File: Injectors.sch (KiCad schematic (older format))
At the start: 36 parts, among them Q1 435M9395, Q2 435M9395, Q3 435M9395, Q4 435M9395, Q5 435M9395, Q6 435M9395

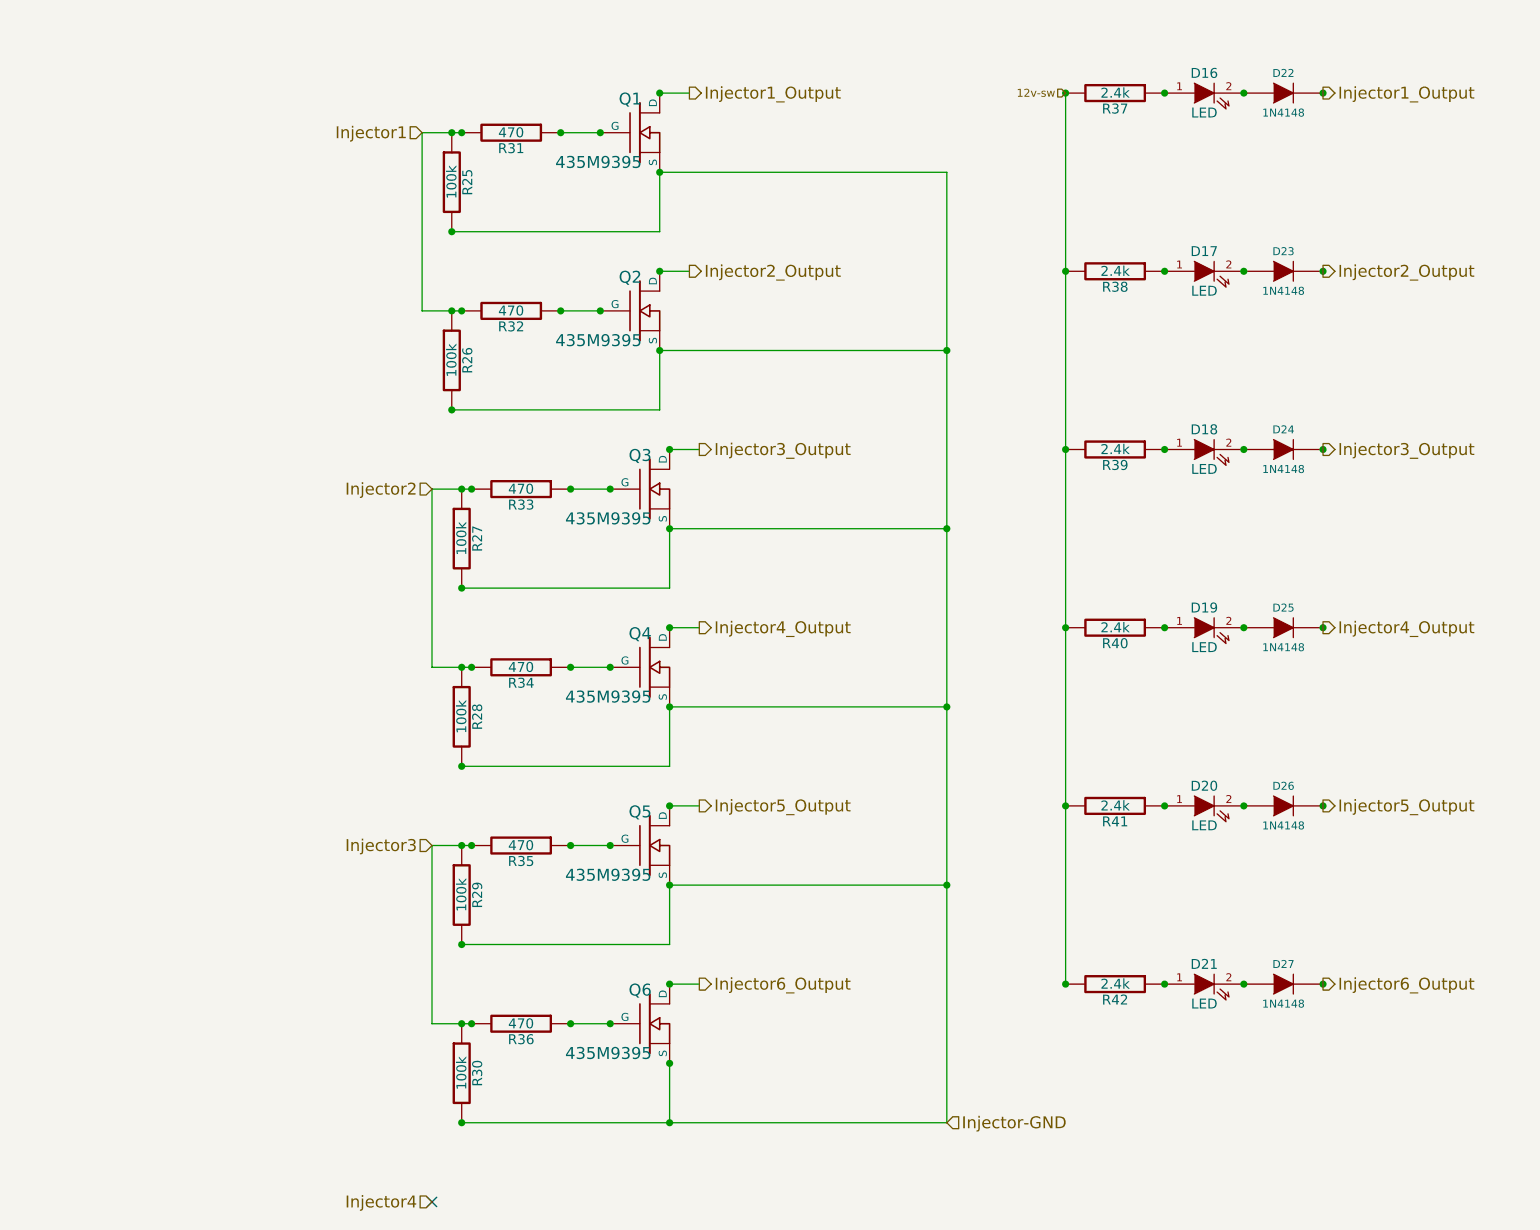
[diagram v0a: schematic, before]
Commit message: Redesigned schematics and board
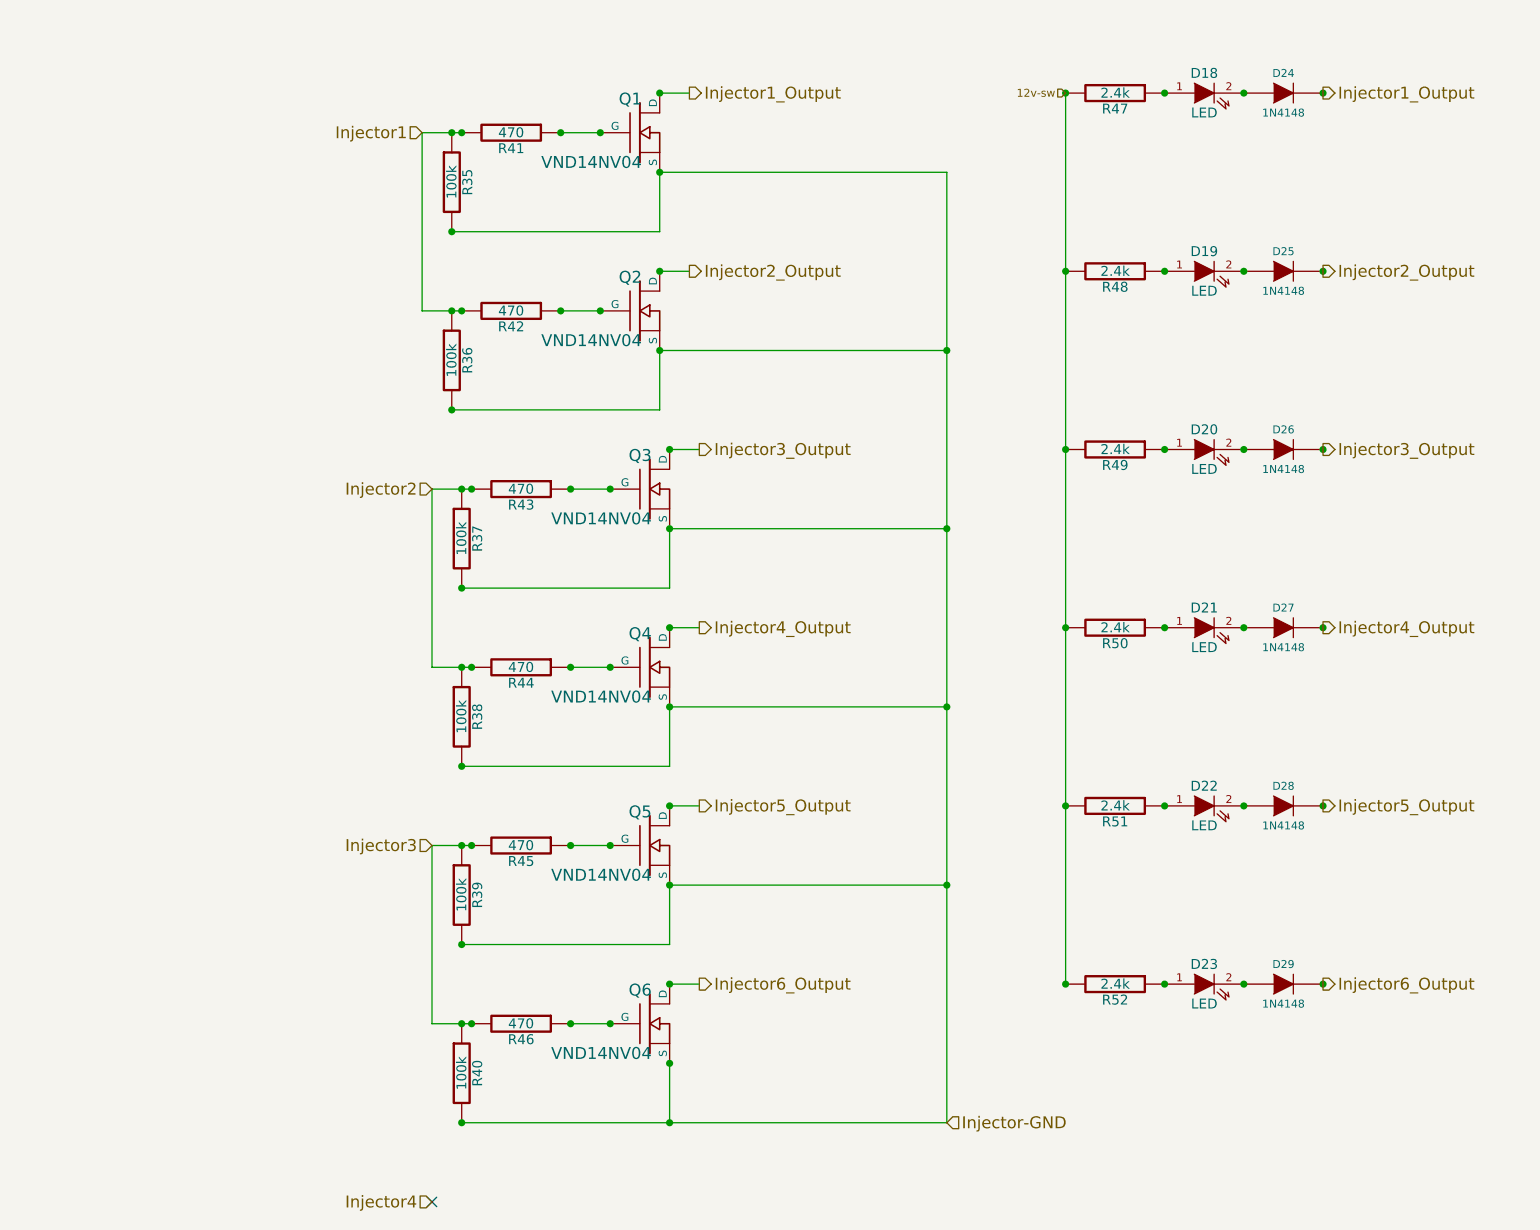
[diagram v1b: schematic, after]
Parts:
- Q1, Q2, Q3, Q4, Q5, Q6: value 435M9395 -> VND14NV04
- renumbered D16 to D18, D17 to D19, D18 to D20, D19 to D21, D20 to D22, D21 to D23, D22 to D24, D23 to D25, D24 to D26, D25 to D27, D26 to D28, D27 to D29, R25 to R35, R26 to R36, R27 to R37, R28 to R38, R29 to R39, R30 to R40, R31 to R41, R32 to R42, R33 to R43, R34 to R44, R35 to R45, R36 to R46, R37 to R47, R38 to R48, R39 to R49, R40 to R50, R41 to R51, R42 to R52
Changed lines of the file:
@@
-EESchema Schematic File Version 2  date Thu 19 Jan 2012 12:17:41 AM EST
+EESchema Schematic File Version 2  date Fri 20 Jan 2012 02:23:37 PM EST
 LIBS:power
 LIBS:device
@@
 Sheet 3 7
 Title "Injector Drivers"
-Date "19 jan 2012"
+Date "20 jan 2012"
 Rev "A"
 Comp "Jaguar board for FreeEMS"
@@
 Injector3
 $Comp
-L DIODE D27
+L DIODE D29
 U 1 1 4F178496
 P 7100 5750
-F 0 "D27" H 7100 5850 40  0000 C CNN
+F 0 "D29" H 7100 5850 40  0000 C CNN
 F 1 "1N4148" H 7100 5650 40  0000 C CNN
 	1    7100 5750
@@
 $EndComp
 $Comp
-L DIODE D26
+L DIODE D28
 U 1 1 4F17848A
 P 7100 4850
-F 0 "D26" H 7100 4950 40  0000 C CNN
+F 0 "D28" H 7100 4950 40  0000 C CNN
 F 1 "1N4148" H 7100 4750 40  0000 C CNN
 	1    7100 4850
@@
 $EndComp
 $Comp
-L DIODE D25
+L DIODE D27
 U 1 1 4F17847C
 P 7100 3950
-F 0 "D25" H 7100 4050 40  0000 C CNN
+F 0 "D27" H 7100 4050 40  0000 C CNN
 F 1 "1N4148" H 7100 3850 40  0000 C CNN
 	1    7100 3950
@@
 $EndComp
 $Comp
-L DIODE D24
+L DIODE D26
 U 1 1 4F178470
 P 7100 3050
-F 0 "D24" H 7100 3150 40  0000 C CNN
+F 0 "D26" H 7100 3150 40  0000 C CNN
 F 1 "1N4148" H 7100 2950 40  0000 C CNN
 	1    7100 3050
@@
 $EndComp
 $Comp
-L DIODE D23
+L DIODE D25
 U 1 1 4F17845F
 P 7100 2150
-F 0 "D23" H 7100 2250 40  0000 C CNN
+F 0 "D25" H 7100 2250 40  0000 C CNN
 F 1 "1N4148" H 7100 2050 40  0000 C CNN
 	1    7100 2150
@@
 $EndComp
 $Comp
-L DIODE D22
+L DIODE D24
 U 1 1 4F17842F
 P 7100 1250
-F 0 "D22" H 7100 1350 40  0000 C CNN
+F 0 "D24" H 7100 1350 40  0000 C CNN
 F 1 "1N4148" H 7100 1150 40  0000 C CNN
 	1    7100 1250
@@
 $EndComp
 $Comp
-L LED D21
+L LED D23
 U 1 1 4F13818D
 P 6700 5750
-F 0 "D21" H 6700 5850 50  0000 C CNN
+F 0 "D23" H 6700 5850 50  0000 C CNN
 F 1 "LED" H 6700 5650 50  0000 C CNN
 	1    6700 5750
@@
 $EndComp
 $Comp
-L R R42
+L R R52
 U 1 1 4F13818C
 P 6250 5750
-F 0 "R42" V 6330 5750 50  0000 C CNN
+F 0 "R52" V 6330 5750 50  0000 C CNN
 F 1 "2.4k" V 6250 5750 50  0000 C CNN
 	1    6250 5750
@@
 Injector5_Output
 $Comp
-L R R41
+L R R51
 U 1 1 4F138183
 P 6250 4850
-F 0 "R41" V 6330 4850 50  0000 C CNN
+F 0 "R51" V 6330 4850 50  0000 C CNN
 F 1 "2.4k" V 6250 4850 50  0000 C CNN
 	1    6250 4850
@@
 $EndComp
 $Comp
-L LED D20
+L LED D22
 U 1 1 4F138182
 P 6700 4850
-F 0 "D20" H 6700 4950 50  0000 C CNN
+F 0 "D22" H 6700 4950 50  0000 C CNN
 F 1 "LED" H 6700 4750 50  0000 C CNN
 	1    6700 4850
@@
 $EndComp
 $Comp
-L LED D19
+L LED D21
 U 1 1 4F13817C
 P 6700 3950
-F 0 "D19" H 6700 4050 50  0000 C CNN
+F 0 "D21" H 6700 4050 50  0000 C CNN
 F 1 "LED" H 6700 3850 50  0000 C CNN
 	1    6700 3950
@@
 $EndComp
 $Comp
-L R R40
+L R R50
 U 1 1 4F13817B
 P 6250 3950
-F 0 "R40" V 6330 3950 50  0000 C CNN
+F 0 "R50" V 6330 3950 50  0000 C CNN
 F 1 "2.4k" V 6250 3950 50  0000 C CNN
 	1    6250 3950
@@
 Injector3_Output
 $Comp
-L R R39
+L R R49
 U 1 1 4F138176
 P 6250 3050
-F 0 "R39" V 6330 3050 50  0000 C CNN
+F 0 "R49" V 6330 3050 50  0000 C CNN
 F 1 "2.4k" V 6250 3050 50  0000 C CNN
 	1    6250 3050
@@
 $EndComp
 $Comp
-L LED D18
+L LED D20
 U 1 1 4F138175
 P 6700 3050
-F 0 "D18" H 6700 3150 50  0000 C CNN
+F 0 "D20" H 6700 3150 50  0000 C CNN
 F 1 "LED" H 6700 2950 50  0000 C CNN
 	1    6700 3050
@@
 $EndComp
 $Comp
-L LED D17
+L LED D19
 U 1 1 4F13816D
 P 6700 2150
-F 0 "D17" H 6700 2250 50  0000 C CNN
+F 0 "D19" H 6700 2250 50  0000 C CNN
 F 1 "LED" H 6700 2050 50  0000 C CNN
 	1    6700 2150
@@
 $EndComp
 $Comp
-L R R38
+L R R48
 U 1 1 4F13816C
 P 6250 2150
-F 0 "R38" V 6330 2150 50  0000 C CNN
+F 0 "R48" V 6330 2150 50  0000 C CNN
 F 1 "2.4k" V 6250 2150 50  0000 C CNN
 	1    6250 2150
@@
 12v-sw
 $Comp
-L R R37
+L R R47
 U 1 1 4F1380A7
 P 6250 1250
-F 0 "R37" V 6330 1250 50  0000 C CNN
+F 0 "R47" V 6330 1250 50  0000 C CNN
 F 1 "2.4k" V 6250 1250 50  0000 C CNN
 	1    6250 1250
@@
 $EndComp
 $Comp
-L LED D16
+L LED D18
 U 1 1 4F138097
 P 6700 1250
-F 0 "D16" H 6700 1350 50  0000 C CNN
+F 0 "D18" H 6700 1350 50  0000 C CNN
 F 1 "LED" H 6700 1150 50  0000 C CNN
 	1    6700 1250
@@
 $EndComp
 $Comp
-L R R30
+L R R40
 U 1 1 4F0D0591
 P 2950 6200
-F 0 "R30" V 3030 6200 50  0000 C CNN
+F 0 "R40" V 3030 6200 50  0000 C CNN
 F 1 "100k" V 2950 6200 50  0000 C CNN
 	1    2950 6200
@@
 $EndComp
 $Comp
-L R R36
+L R R46
 U 1 1 4F0D0590
 P 3250 5950
-F 0 "R36" V 3330 5950 50  0000 C CNN
+F 0 "R46" V 3330 5950 50  0000 C CNN
 F 1 "470" V 3250 5950 50  0000 C CNN
 	1    3250 5950
@@
 P 3900 5950
 F 0 "Q6" H 3910 6120 60  0000 R CNN
-F 1 "435M9395" H 3910 5800 60  0000 R CNN
+F 1 "VND14NV04" H 3910 5800 60  0000 R CNN
 	1    3900 5950
 	1    0    0    -1
@@
 P 3900 5050
 F 0 "Q5" H 3910 5220 60  0000 R CNN
-F 1 "435M9395" H 3910 4900 60  0000 R CNN
+F 1 "VND14NV04" H 3910 4900 60  0000 R CNN
 	1    3900 5050
 	1    0    0    -1
 $EndComp
 $Comp
-L R R35
+L R R45
 U 1 1 4F0D0585
 P 3250 5050
-F 0 "R35" V 3330 5050 50  0000 C CNN
+F 0 "R45" V 3330 5050 50  0000 C CNN
 F 1 "470" V 3250 5050 50  0000 C CNN
 	1    3250 5050
@@
 $EndComp
 $Comp
-L R R29
+L R R39
 U 1 1 4F0D0584
 P 2950 5300
-F 0 "R29" V 3030 5300 50  0000 C CNN
+F 0 "R39" V 3030 5300 50  0000 C CNN
 F 1 "100k" V 2950 5300 50  0000 C CNN
 	1    2950 5300
@@
 $EndComp
 $Comp
-L R R28
+L R R38
 U 1 1 4F0D0577
 P 2950 4400
-F 0 "R28" V 3030 4400 50  0000 C CNN
+F 0 "R38" V 3030 4400 50  0000 C CNN
 F 1 "100k" V 2950 4400 50  0000 C CNN
 	1    2950 4400
@@
 $EndComp
 $Comp
-L R R34
+L R R44
 U 1 1 4F0D0576
 P 3250 4150
-F 0 "R34" V 3330 4150 50  0000 C CNN
+F 0 "R44" V 3330 4150 50  0000 C CNN
 F 1 "470" V 3250 4150 50  0000 C CNN
 	1    3250 4150
@@
 P 3900 4150
 F 0 "Q4" H 3910 4320 60  0000 R CNN
-F 1 "435M9395" H 3910 4000 60  0000 R CNN
+F 1 "VND14NV04" H 3910 4000 60  0000 R CNN
 	1    3900 4150
 	1    0    0    -1
 $EndComp
 $Comp
-L R R27
+L R R37
 U 1 1 4F0D0559
 P 2950 3500
-F 0 "R27" V 3030 3500 50  0000 C CNN
+F 0 "R37" V 3030 3500 50  0000 C CNN
 F 1 "100k" V 2950 3500 50  0000 C CNN
 	1    2950 3500
@@
 $EndComp
 $Comp
-L R R33
+L R R43
 U 1 1 4F0D0558
 P 3250 3250
-F 0 "R33" V 3330 3250 50  0000 C CNN
+F 0 "R43" V 3330 3250 50  0000 C CNN
 F 1 "470" V 3250 3250 50  0000 C CNN
 	1    3250 3250
@@
 P 3900 3250
 F 0 "Q3" H 3910 3420 60  0000 R CNN
-F 1 "435M9395" H 3910 3100 60  0000 R CNN
+F 1 "VND14NV04" H 3910 3100 60  0000 R CNN
 	1    3900 3250
 	1    0    0    -1
 $EndComp
 $Comp
-L R R26
+L R R36
 U 1 1 4F0D0547
 P 2900 2600
-F 0 "R26" V 2980 2600 50  0000 C CNN
+F 0 "R36" V 2980 2600 50  0000 C CNN
 F 1 "100k" V 2900 2600 50  0000 C CNN
 	1    2900 2600
@@
 $EndComp
 $Comp
-L R R32
+L R R42
 U 1 1 4F0D0546
 P 3200 2350
-F 0 "R32" V 3280 2350 50  0000 C CNN
+F 0 "R42" V 3280 2350 50  0000 C CNN
 F 1 "470" V 3200 2350 50  0000 C CNN
 	1    3200 2350
@@
 P 3850 2350
 F 0 "Q2" H 3860 2520 60  0000 R CNN
-F 1 "435M9395" H 3860 2200 60  0000 R CNN
+F 1 "VND14NV04" H 3860 2200 60  0000 R CNN
 	1    3850 2350
 	1    0    0    -1
@@
 P 3850 1450
 F 0 "Q1" H 3860 1620 60  0000 R CNN
-F 1 "435M9395" H 3860 1300 60  0000 R CNN
+F 1 "VND14NV04" H 3860 1300 60  0000 R CNN
 	1    3850 1450
 	1    0    0    -1
 $EndComp
 $Comp
-L R R31
+L R R41
 U 1 1 4F062C55
 P 3200 1450
-F 0 "R31" V 3280 1450 50  0000 C CNN
+F 0 "R41" V 3280 1450 50  0000 C CNN
 F 1 "470" V 3200 1450 50  0000 C CNN
 	1    3200 1450
@@
 $EndComp
 $Comp
-L R R25
+L R R35
 U 1 1 4F062C4D
 P 2900 1700
-F 0 "R25" V 2980 1700 50  0000 C CNN
+F 0 "R35" V 2980 1700 50  0000 C CNN
 F 1 "100k" V 2900 1700 50  0000 C CNN
 	1    2900 1700
